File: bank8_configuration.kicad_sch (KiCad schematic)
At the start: 19 parts, among them U1 ECP5-BGA256, U10 W25Q32JVSS

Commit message: schematic wip
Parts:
- removed TP26, TP27: TestPoint, TestPoint:TestPoint_Pad_D1.0mm, symbol Connector:TestPoint
- added R114, R115, R116, R18: 10k, Resistor_SMD:R_0402_1005Metric, symbol Device:R
- added unit 1 of U1
- C55: value 0.1uF -> 100nF
- U10: value W25Q32JVSS -> W25Q16; Part Number W25Q32JVSSIQ -> W25Q16JVSSIQ
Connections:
- net +3V3: now also R114.1, R115.1, R116.1, R18.1
- net D0: now also R18.2
- net D1: now also R114.2
- net D2: now also R115.2
- net D3: now also R116.2
- net GND: now also U1.A1 (GND_1), U1.A16 (GND_2), U1.D15 (GND_4), U1.D2 (GND_3), U1.F8 (GND_5), U1.F9 (GND_6), U1.G10 (GND_8), U1.G8 (GND_7), U1.H1 (GND_9), U1.H10 (GND_12), U1.H16 (GND_13), U1.H8 (GND_10), U1.H9 (GND_11), U1.J10 (GND_16), U1.J8 (GND_14), U1.J9 (GND_15), U1.K10 (GND_21), U1.K6 (GND_17), U1.K7 (GND_18), U1.K8 (GND_19), U1.K9 (GND_20), U1.N15 (GND_23), U1.N2 (GND_22), U1.T1 (GND_24), U1.T12 (GND_26), U1.T16 (GND_27), U1.T5 (GND_25)
- new net +1V1: U1.G6 (VCC_1), U1.G7 (VCC_2), U1.G9 (VCC_3), U1.L10 (VCC_6), U1.L8 (VCC_4), U1.L9 (VCC_5)
- new net +2V5: U1.G11 (VCCAUX_1), U1.L7 (VCCAUX_2)
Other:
- note added: "Select MSPI mode, so the ECP5 will self-configure from flash."
- note added: "VCC: 2.7 to 3.6 V"
- note removed: "By default, select MSPI mode, so the ECP5 will self-configure from flash."
- moved on the sheet: C55, R37, R38, R39, R40, R41, R42, R43, R44, TP28, TP29, TP30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

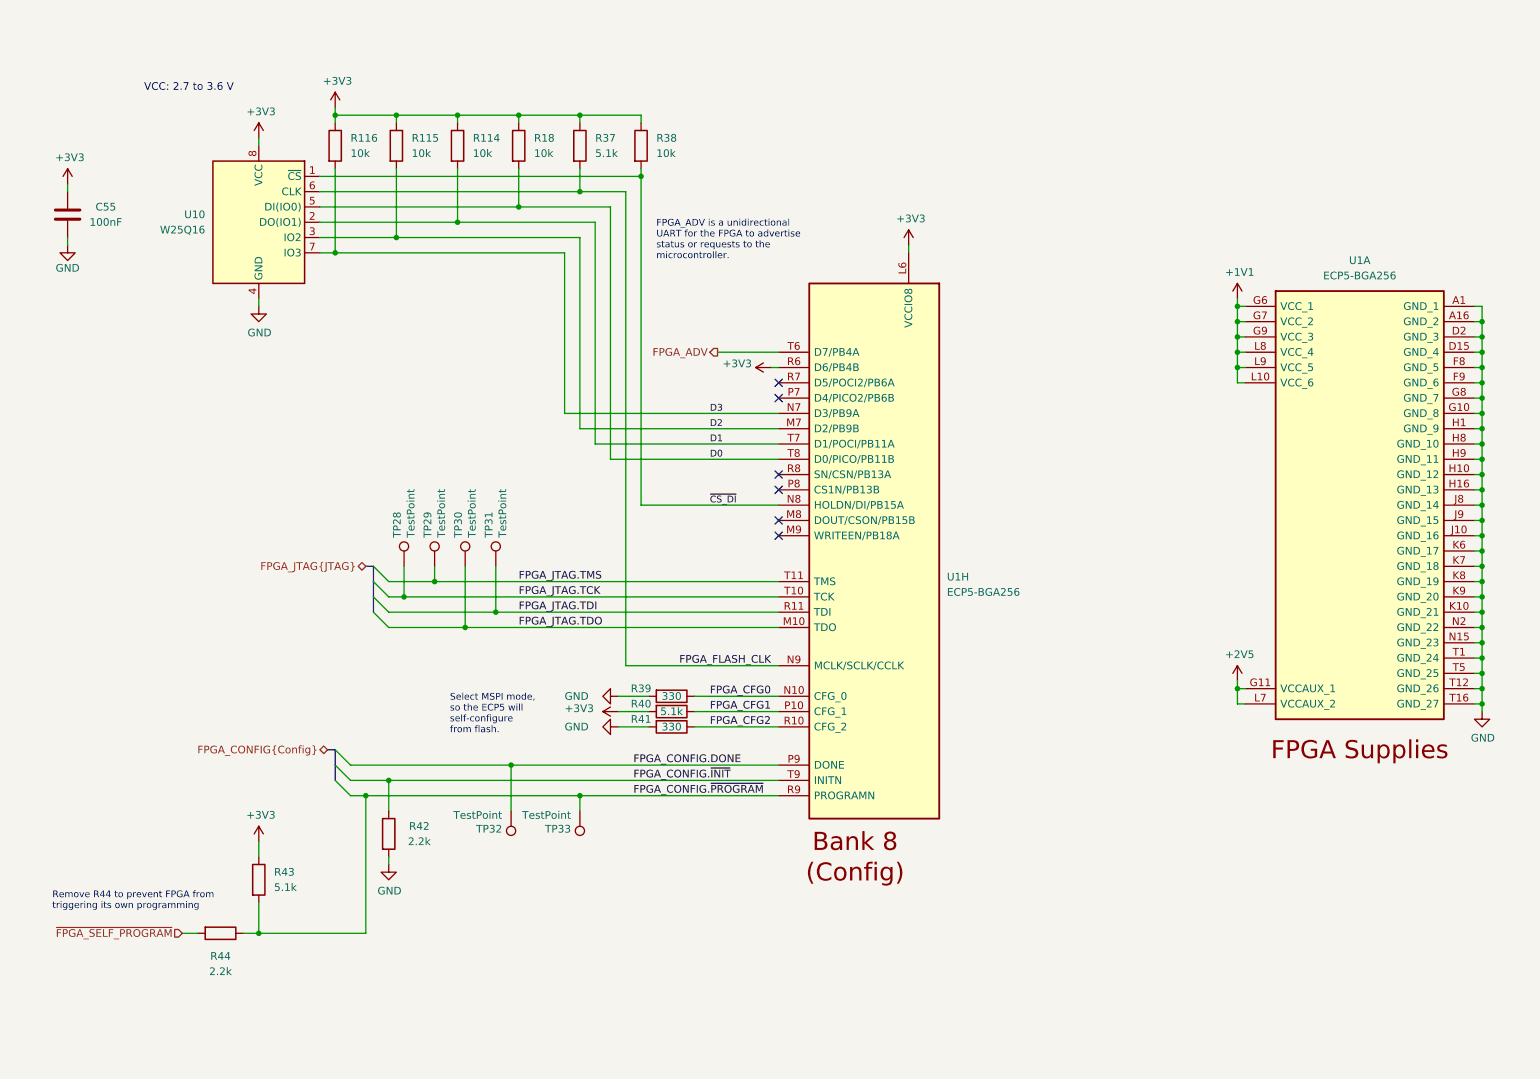
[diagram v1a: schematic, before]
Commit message: add regulator for analog 3.3 V supply
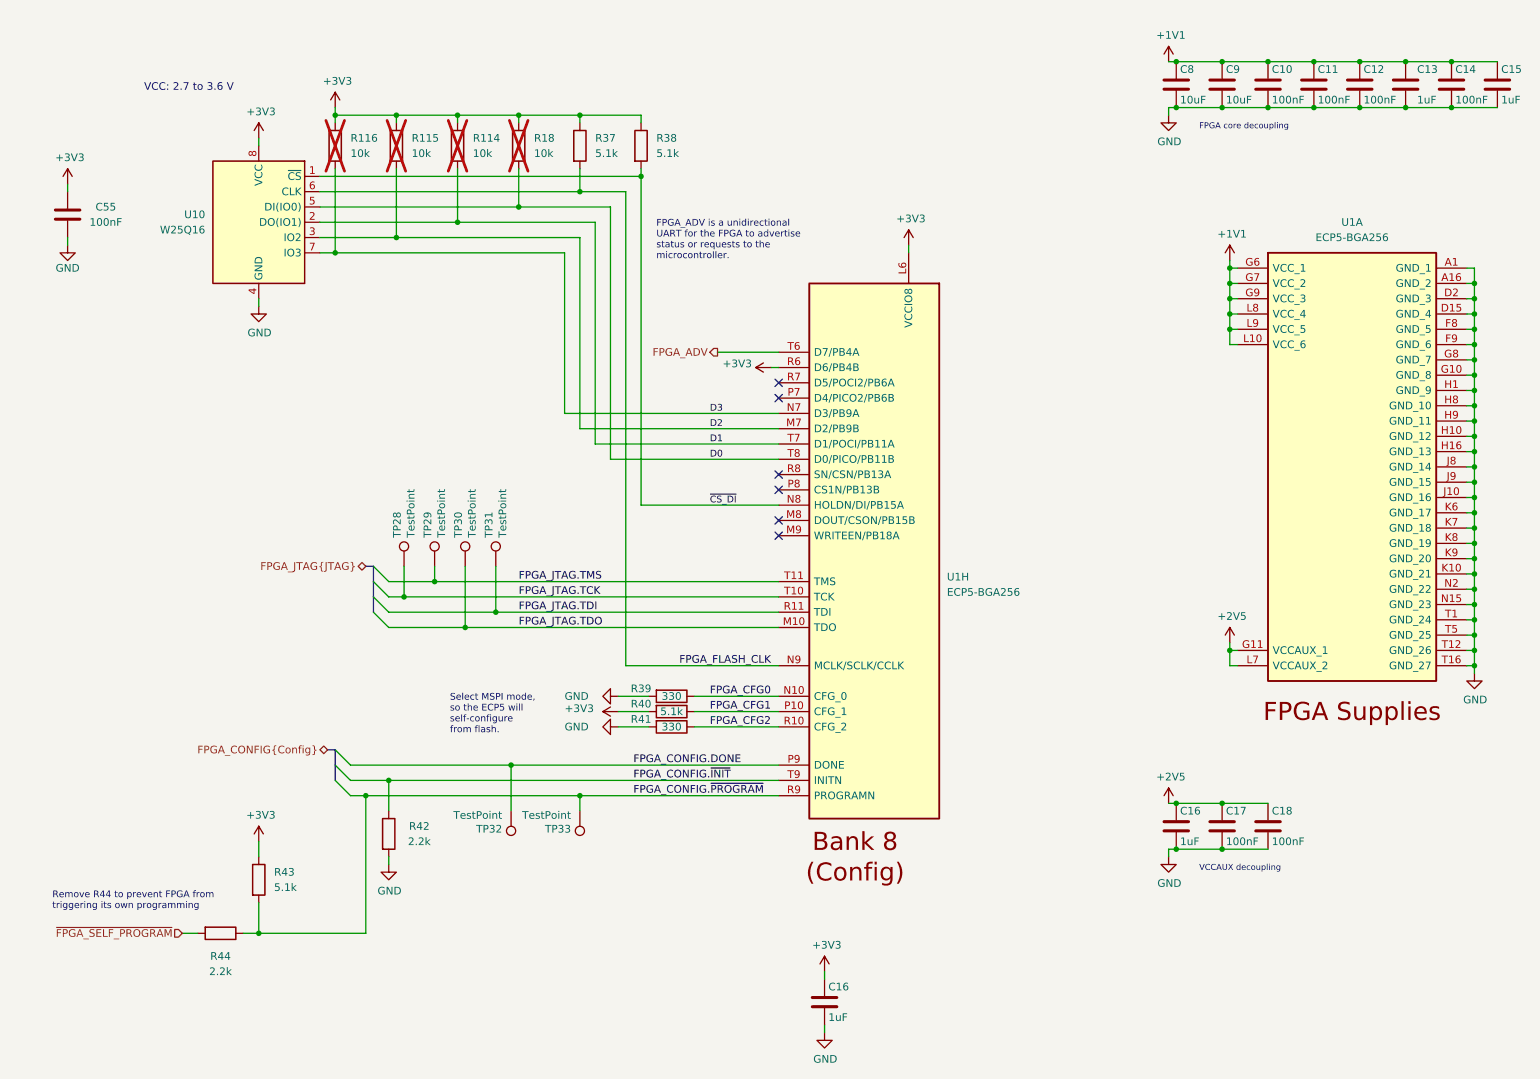
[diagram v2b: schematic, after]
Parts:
- added C10, C11, C12, C14, C17, C18: 100nF, Capacitor_SMD:C_0402_1005Metric, symbol Device:C
- added C13, C15, C16 (x2): 1uF, Capacitor_SMD:C_0402_1005Metric, symbol Device:C
- added C8, C9: 10uF, Capacitor_SMD:C_0603_1608Metric, symbol Device:C
- R114, R115, R116, R18: now not fitted
- R38: value 10k -> 5.1k; Part Number RC0402JR-0710KL -> RC0402JR-075K1L
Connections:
- net +1V1: now also C10.1, C11.1, C12.1, C13.1, C14.1, C15.1, C8.1, C9.1
- net +2V5: now also C16.1, C17.1, C18.1
- net +3V3: now also C16.1
- net GND: now also C10.2, C11.2, C12.2, C13.2, C14.2, C15.2, C16.2, C16.2, C17.2, C18.2, C8.2, C9.2
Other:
- note added: "FPGA core decoupling"
- note added: "VCCAUX decoupling"
- moved on the sheet: U1A

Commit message: complete initial layout
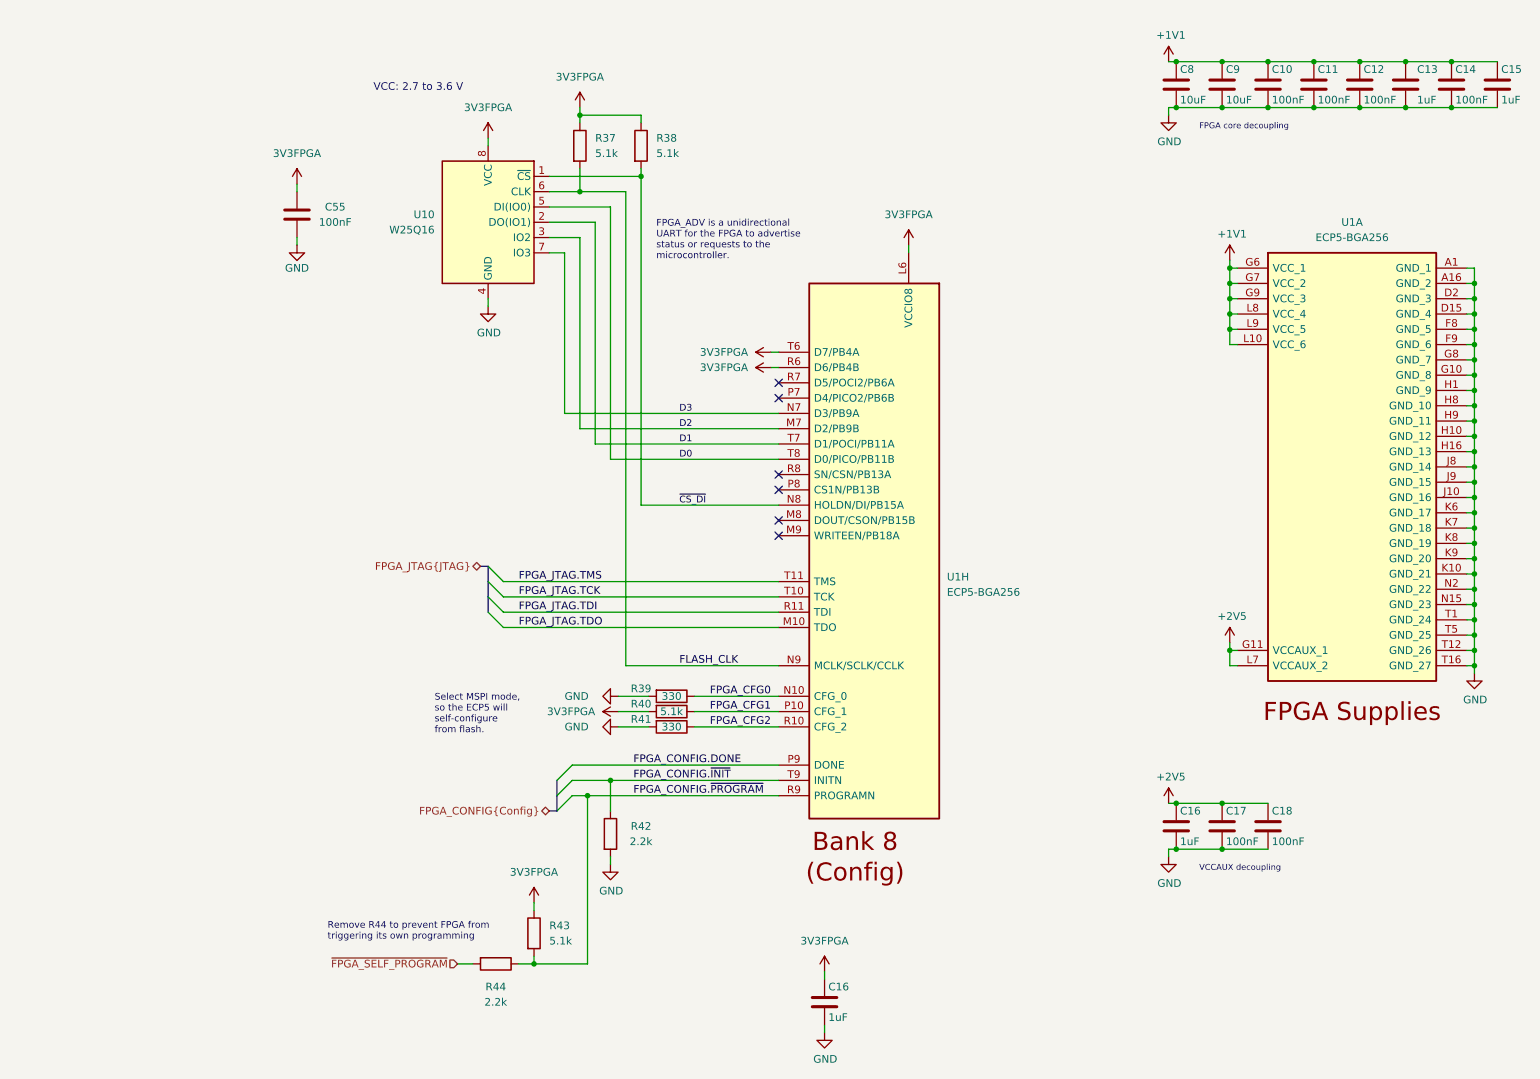
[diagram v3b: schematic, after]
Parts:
- removed R114, R115, R116, R18: 10k, Resistor_SMD:R_0402_1005Metric, symbol Device:R
- removed TP28, TP29, TP30, TP31, TP32, TP33: TestPoint, TestPoint:TestPoint_Pad_D1.0mm, symbol Connector:TestPoint
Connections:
- net FPGA_ADV is gone; now on net 3V3FPGA: U1.T6 (D7/PB4A)
- net +3V3 renamed 3V3FPGA
- net FPGA_FLASH_CLK renamed FLASH_CLK
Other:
- moved on the sheet: C55, R42, R43, R44, U10
